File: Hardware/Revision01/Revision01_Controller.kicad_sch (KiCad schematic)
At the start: 8 parts, among them U1 NUCLEO-L476RG

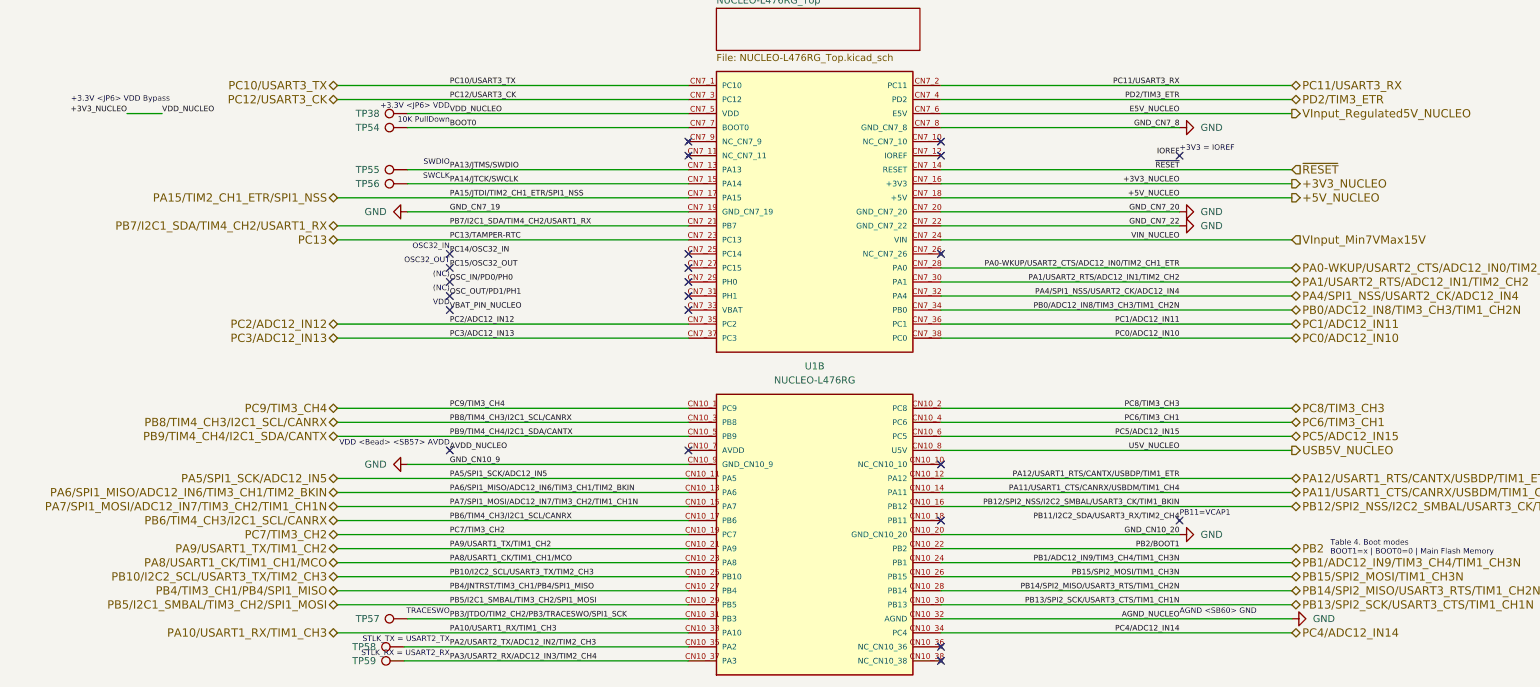
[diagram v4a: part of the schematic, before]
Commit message: . Fixed MCU sheet pins neglecting Button1, Button2, and LED2.
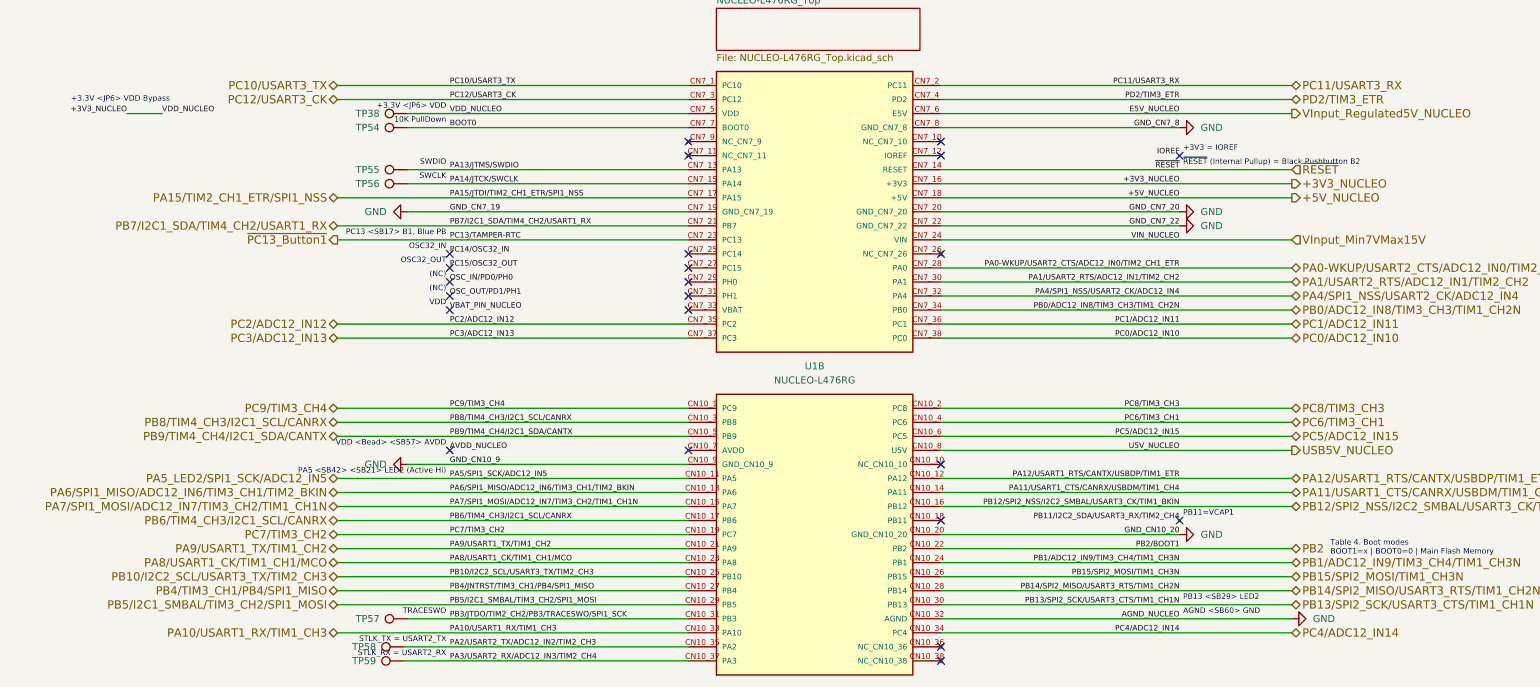
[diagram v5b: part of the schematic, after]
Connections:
- net PA5/SPI1_SCK/ADC12_IN5 renamed PA5_LED2/SPI1_SCK/ADC12_IN5
- net PB13/SPI2_SCK/USART3_CTS/TIM1_CH1N renamed PB13/SPI2_SCK/USART3_CTS/TIM1_CH1N
- net PC13 renamed ~{PC13_Button1}
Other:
- note added: "PA5 <SB42> <SB21> LED2 (Active Hi)"
- note added: "PB13 <SB29> LED2"
- note added: "PC13 <SB17> B1, Blue PB"
- note added: "~{RESET} (Internal Pullup) = Black Pushbutton B2"
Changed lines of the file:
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@@
 	(text "SWDIO\n"
 		(exclude_from_sim no)
-		(at 86.995 58.42 0)
+		(at 86.36 58.42 0)
 		(effects
 			(font
@@
 	(text "VDD"
 		(exclude_from_sim no)
-		(at 86.995 83.82 0)
+		(at 86.36 83.82 0)
 		(effects
 			(font
@@
 	(text "(NC)\n"
 		(exclude_from_sim no)
-		(at 86.995 78.74 0)
+		(at 86.36 78.74 0)
 		(effects
 			(font
@@
 	(text "PB11=VCAP1"
 		(exclude_from_sim no)
-		(at 219.075 121.92 0)
+		(at 219.71 121.92 0)
+		(effects
+			(font
+				(size 1 1)
+			)
+			(justify left)
+		)
+	)
+	(text "PB13 <SB29> LED2"
+		(exclude_from_sim no)
+		(at 219.71 137.16 0)
 		(effects
 			(font
@@
 	(text "(NC)"
 		(exclude_from_sim no)
-		(at 86.995 81.28 0)
+		(at 86.36 81.28 0)
+		(effects
+			(font
+				(size 1 1)
+			)
+			(justify right)
+		)
+	)
+	(text "PA5 <SB42> <SB21> LED2 (Active Hi)"
+		(exclude_from_sim no)
+		(at 86.36 114.3 0)
 		(effects
 			(font
@@
 		)
 	)
+	(text ""
+		(exclude_from_sim no)
+		(at 135.89 153.67 0)
+		(effects
+			(font
+				(size 1 1)
+			)
+			(justify left)
+		)
+	)
+	(text "~{RESET} (Internal Pullup) = Black Pushbutton B2"
+		(exclude_from_sim no)
+		(at 219.71 58.42 0)
+		(effects
+			(font
+				(size 1 1)
+			)
+			(justify left)
+		)
+	)
 	(text "OSC32_IN\n"
 		(exclude_from_sim no)
-		(at 86.995 73.66 0)
+		(at 86.36 73.66 0)
 		(effects
 			(font
@@
 	(text "SWCLK"
 		(exclude_from_sim no)
-		(at 86.995 60.96 0)
+		(at 86.36 60.96 0)
 		(effects
 			(font
@@
 	(text "OSC32_OUT\n"
 		(exclude_from_sim no)
-		(at 86.995 76.2 0)
+		(at 86.36 76.2 0)
+		(effects
+			(font
+				(size 1 1)
+			)
+			(justify right)
+		)
+	)
+	(text "PC13 <SB17> B1, Blue PB"
+		(exclude_from_sim no)
+		(at 86.36 71.12 0)
 		(effects
 			(font
@@
 	(text "STLK_TX = USART2_TX"
 		(exclude_from_sim no)
-		(at 86.995 144.78 0)
+		(at 86.36 144.78 0)
 		(effects
 			(font
@@
 	(text "10K PullDown"
 		(exclude_from_sim no)
-		(at 86.995 50.8 0)
+		(at 86.36 50.8 0)
 		(effects
 			(font
@@
 	(text "VDD <Bead> <SB57> AVDD"
 		(exclude_from_sim no)
-		(at 86.995 109.22 0)
+		(at 86.36 109.22 0)
 		(effects
 			(font
@@
 	(text "AGND <SB60> GND"
 		(exclude_from_sim no)
-		(at 219.075 139.7 0)
+		(at 219.71 139.7 0)
 		(effects
 			(font
@@
 	(text "+3V3 = IOREF"
 		(exclude_from_sim no)
-		(at 219.075 55.88 0)
+		(at 219.71 55.88 0)
 		(effects
 			(font
@@
 	(text "TRACESWO"
 		(exclude_from_sim no)
-		(at 86.995 139.7 0)
+		(at 86.36 139.7 0)
 		(effects
 			(font
@@
 	(text "STLK_RX = USART2_RX"
 		(exclude_from_sim no)
-		(at 86.995 147.32 0)
+		(at 86.36 147.32 0)
 		(effects
 			(font
@@
 	(text "+3.3V <JP6> VDD"
 		(exclude_from_sim no)
-		(at 86.995 48.26 0)
+		(at 86.36 48.26 0)
 		(effects
 			(font
@@
 		)
 	)
-	(hierarchical_label "PA5{slash}SPI1_SCK{slash}ADC12_IN5"
+	(hierarchical_label "PA5_LED2/SPI1_SCK/ADC12_IN5"
 		(shape bidirectional)
 		(at 66.675 115.57 180)
@@
 		)
 	)
-	(hierarchical_label "PC13"
-		(shape bidirectional)
+	(hierarchical_label "~{PC13_Button1}"
+		(shape output)
 		(at 66.675 72.39 180)
 		(effects
@@
 		)
 	)
-	(hierarchical_label "PB13{slash}SPI2_SCK{slash}USART3_CTS{slash}TIM1_CH1N"
+	(hierarchical_label "PB13/SPI2_SCK/USART3_CTS/TIM1_CH1N"
 		(shape bidirectional)
 		(at 239.395 138.43 0)

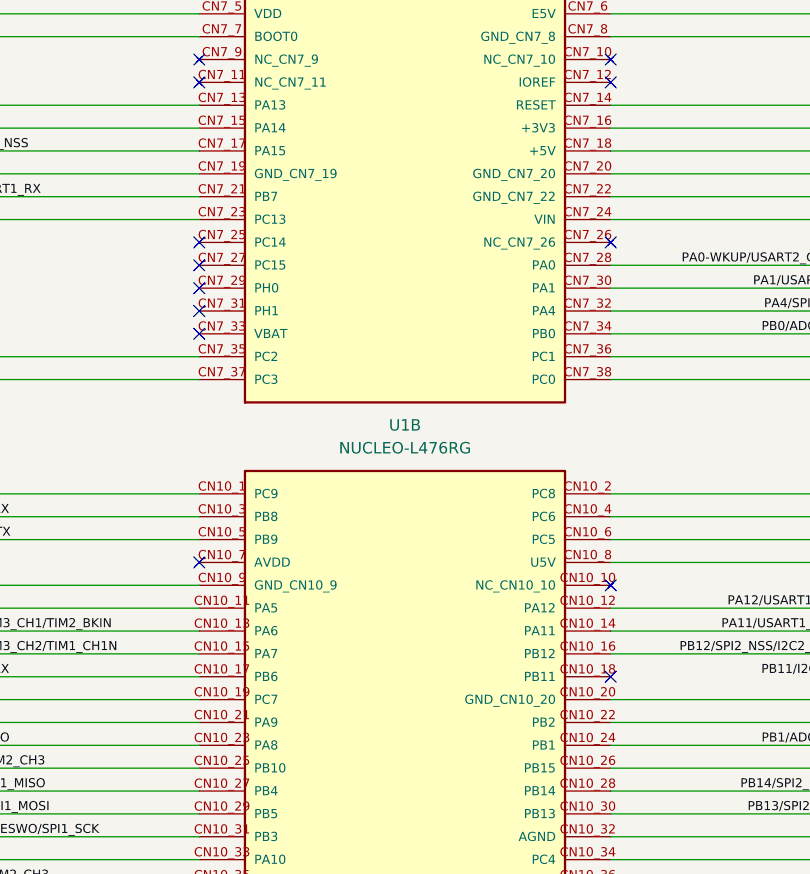
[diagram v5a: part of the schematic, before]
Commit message: neated up the circuit - done wire-accross sheets - done Ensure all components have footprints - done Create net classes - DONE 	POWER 	GND 	SPI 	GPIO
Add in new components into BOM
	- Power switch, exclude from BOM - DONE - added component to switch. Not sure how to get it to work
	- Add in the resistors in parallel and series. for SPI busses - Done(PENDING whether to take series resistors out)
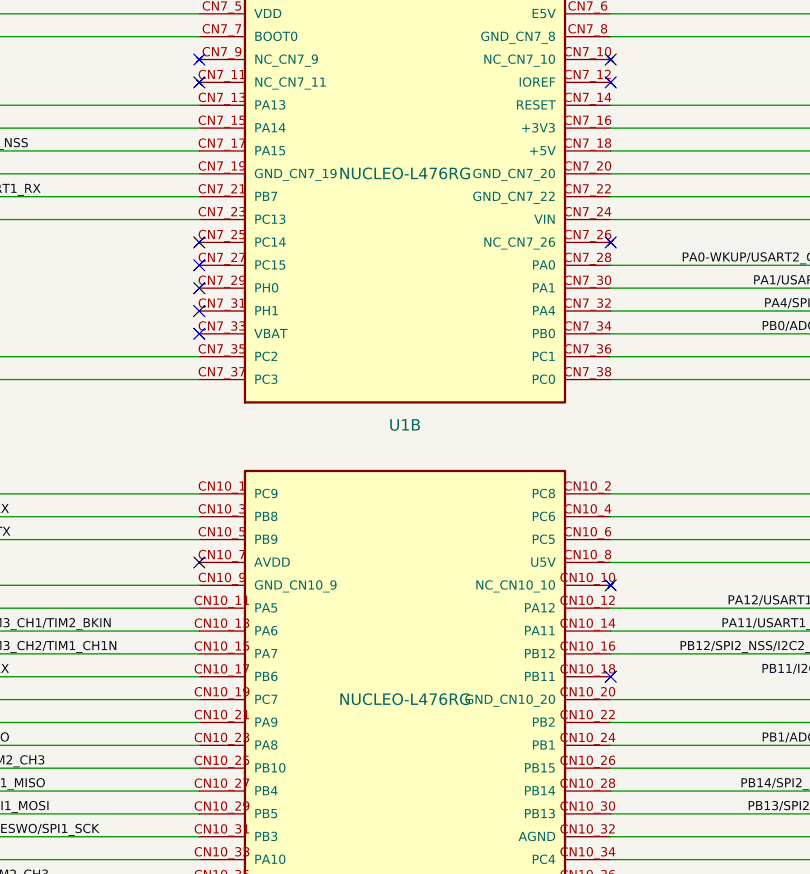
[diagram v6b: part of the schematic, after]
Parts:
- TP38, TP54, TP55, TP56, TP57, TP58, TP59: footprint (none) -> TestPoint:TestPoint_THTPad_1.0x1.0mm_Drill0.5mm
- U1: Distributor link (none) -> https://www.digikey.ca/en/products/detail/stmicroelectronic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; Manufacturer Part Number (none) -> NUCLEO-L476RG; now left out of the parts list
